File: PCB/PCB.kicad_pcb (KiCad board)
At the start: 2 copper layers, 26 x 49 mm, 8 parts, among them IC1 MSPM0G3507SPTR, J1 ICS43434 Breakout, J2 MAX98357_Breakout, J4 LED_Header, J5 MSPM0 Programming Header, J6 USBC_Power_Breakout, U2 254

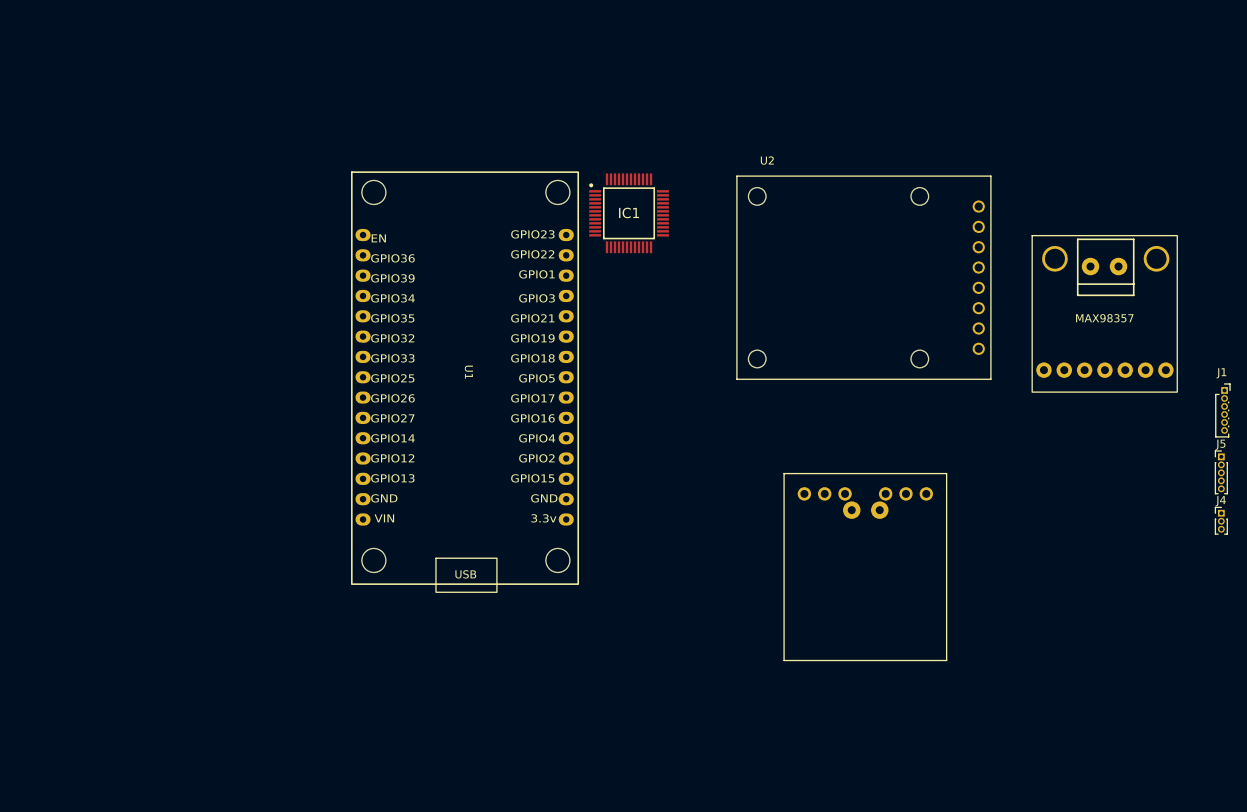
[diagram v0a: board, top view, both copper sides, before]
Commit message: all symbols and footprints
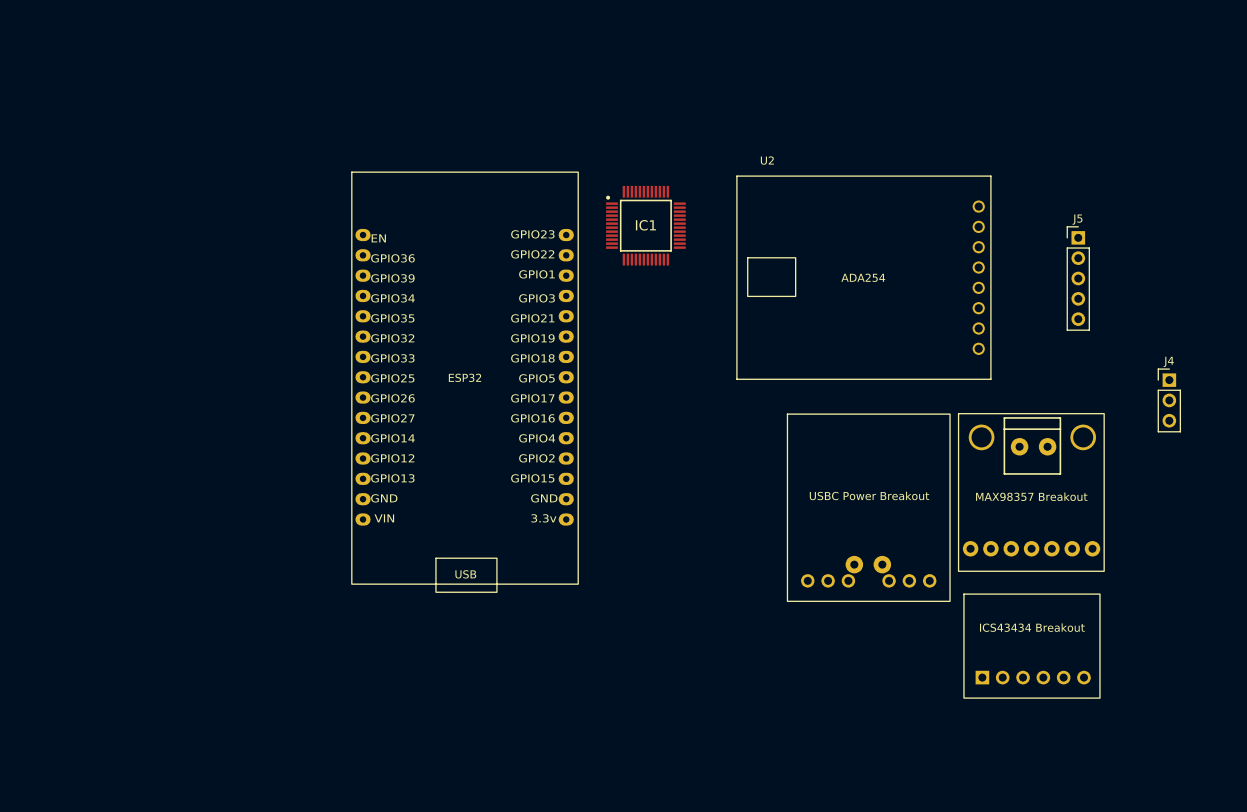
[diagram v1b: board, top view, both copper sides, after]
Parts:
- IC1: value MSPM0G3507SPTR -> QFP50P900X900X160-48N
- J1: footprint Connector_PinSocket_1.00mm:PinSocket_1x06_P1.00mm_Vertical -> SpinnyKitty:ICS43434 Breakout
- J4: footprint Connector_PinHeader_1.00mm:PinHeader_1x03_P1.00mm_Vertical -> Connector_PinHeader_2.54mm:PinHeader_1x03_P2.54mm_Vertical
- J5: footprint Connector_PinHeader_1.00mm:PinHeader_1x05_P1.00mm_Vertical -> Connector_PinHeader_2.54mm:PinHeader_1x05_P2.54mm_Vertical
- moved J1 38.2 mm to (139.5, 89.0)
- moved J5 32.7 mm to (145.3, 40.2)
- moved J2 24.1 mm to (139.4, 66.1)
- moved J4 17.9 mm to (156.7, 58.0)
- moved J6 6.82 mm to (119.1, 81.1), turned to 0 degrees
- moved IC1 2.61 mm to (91.2, 38.7)
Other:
- board outline removed

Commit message: schematic for on board power system
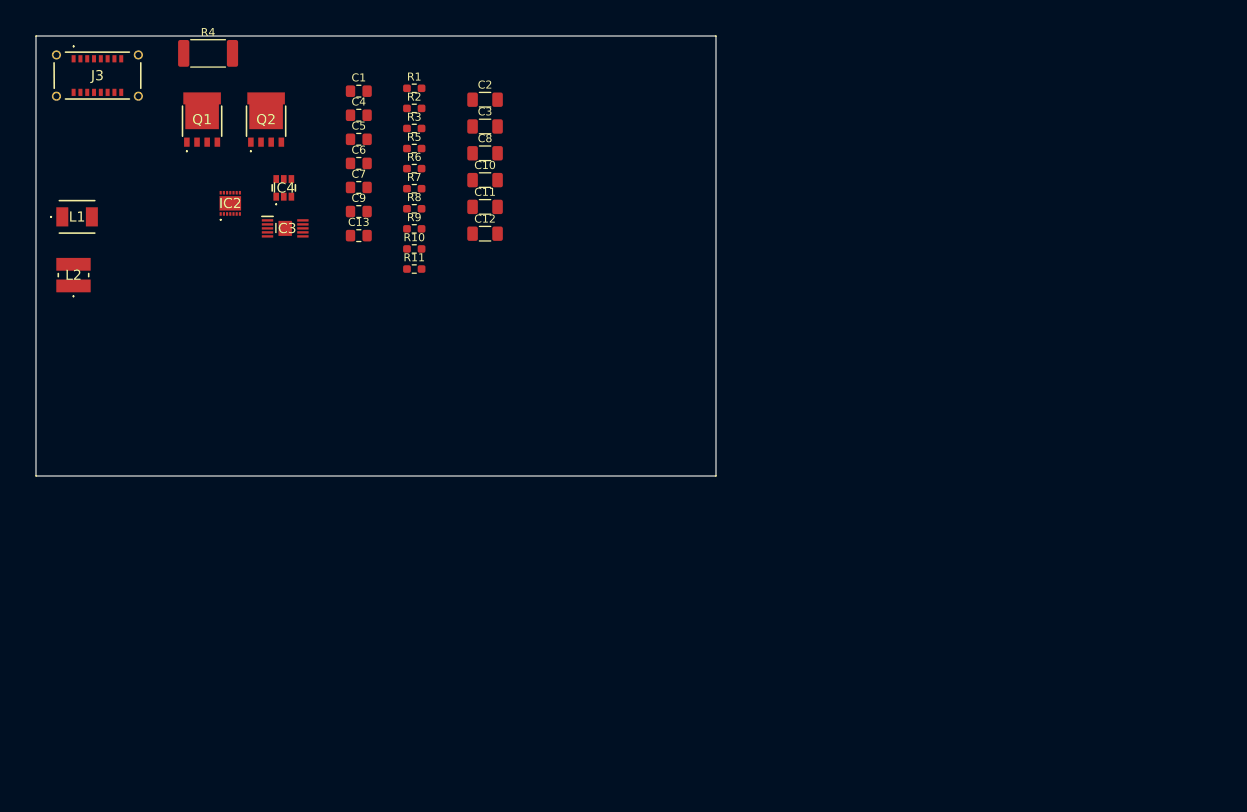
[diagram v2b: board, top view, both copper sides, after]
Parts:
- removed IC1: QFP50P900X900X160-48N, SpinnyKitty:MSPM0G3507SPTR
- removed J1: ICS43434 Breakout, SpinnyKitty:ICS43434 Breakout
- removed J2: MAX98357_Breakout, SpinnyKitty:MAX98357
- removed J4: LED_Header, Connector_PinHeader_2.54mm:PinHeader_1x03_P2.54mm_Vertical
- removed J5: MSPM0 Programming Header, Connector_PinHeader_2.54mm:PinHeader_1x05_P2.54mm_Vertical
- removed J6: USBC_Power_Breakout, SpinnyKitty:USBC_POWER_BREAKOUT
- removed U1: ~, SpinnyKitty:ESP32_30pin
- removed U2: 254, SpinnyKitty:MODULE_254
- added C1: 1uF, Capacitor_SMD:C_0805_2012Metric_Pad1.18x1.45mm_HandSolder, F.Cu at (55.4, 21.9)
- added C10: 10uF, Capacitor_SMD:C_1206_3216Metric_Pad1.33x1.80mm_HandSolder, F.Cu at (71.1, 33.0)
- added C11: 22uF, Capacitor_SMD:C_1206_3216Metric_Pad1.33x1.80mm_HandSolder, F.Cu at (71.1, 36.4)
- added C12: 22uF, Capacitor_SMD:C_1206_3216Metric_Pad1.33x1.80mm_HandSolder, F.Cu at (71.1, 39.7)
- added C13: 100nF, Capacitor_SMD:C_0805_2012Metric_Pad1.18x1.45mm_HandSolder, F.Cu at (55.4, 40.0)
- added C2: 10uF, Capacitor_SMD:C_1206_3216Metric_Pad1.33x1.80mm_HandSolder, F.Cu at (71.1, 23.0)
- added C3: 10uF, Capacitor_SMD:C_1206_3216Metric_Pad1.33x1.80mm_HandSolder, F.Cu at (71.1, 26.3)
- added C4: 4.7uF, Capacitor_SMD:C_0805_2012Metric_Pad1.18x1.45mm_HandSolder, F.Cu at (55.4, 24.9)
- added C5: 0.1uF, Capacitor_SMD:C_0805_2012Metric_Pad1.18x1.45mm_HandSolder, F.Cu at (55.4, 27.9)
- added C6: 1uF, Capacitor_SMD:C_0805_2012Metric_Pad1.18x1.45mm_HandSolder, F.Cu at (55.4, 30.9)
- added C7: 10nF, Capacitor_SMD:C_0805_2012Metric_Pad1.18x1.45mm_HandSolder, F.Cu at (55.4, 33.9)
- added C8: 22uF, Capacitor_SMD:C_1206_3216Metric_Pad1.33x1.80mm_HandSolder, F.Cu at (71.1, 29.7)
- added C9: 10pF, Capacitor_SMD:C_0805_2012Metric_Pad1.18x1.45mm_HandSolder, F.Cu at (55.4, 36.9)
- added IC2: AP33771CFBZ-13-FA01, SpinnyKitty:AP33771CFBZ13FA01, F.Cu at (39.3, 35.9)
- added IC3: LT8609EMSE#PBF, SpinnyKitty:SOP50P490X110-11N, F.Cu at (46.1, 39.0)
- added IC4: AP63203WU-7, SpinnyKitty:AP63203WU7, F.Cu at (46.0, 34.0)
- added J3: UJ20-C-V-SMT-TR-68, SpinnyKitty:UJ20CVSMTTR68, F.Cu at (22.7, 19.9)
- added L1: 2.2uH, SpinnyKitty:PM5402222NLT, F.Cu at (20.1, 37.6)
- added L2: 3.9uH, SpinnyKitty:SRR3818A3R9Y, F.Cu at (19.7, 44.9)
- added Q1: PSMN2R6-30YLC,115, SpinnyKitty:PSMN2R630YLC115, F.Cu at (35.8, 25.6)
- added Q2: PSMN2R6-30YLC,115, SpinnyKitty:PSMN2R630YLC115, F.Cu at (43.8, 25.6)
- added R1: 5.1k, Resistor_SMD:R_0603_1608Metric_Pad0.98x0.95mm_HandSolder, F.Cu at (62.3, 21.5)
- added R10: 187k, Resistor_SMD:R_0603_1608Metric_Pad0.98x0.95mm_HandSolder, F.Cu at (62.3, 41.6)
- added R11: 1M, Resistor_SMD:R_0603_1608Metric_Pad0.98x0.95mm_HandSolder, F.Cu at (62.3, 44.1)
- added R2: 5.1k, Resistor_SMD:R_0603_1608Metric_Pad0.98x0.95mm_HandSolder, F.Cu at (62.3, 24.0)
- added R3: 6.2k, Resistor_SMD:R_0603_1608Metric_Pad0.98x0.95mm_HandSolder, F.Cu at (62.3, 26.6)
- added R4: 5m, Resistor_SMD:R_2512_6332Metric_Pad1.40x3.35mm_HandSolder, F.Cu at (36.5, 17.2)
- added R5: 200, Resistor_SMD:R_0603_1608Metric_Pad0.98x0.95mm_HandSolder, F.Cu at (62.3, 29.1)
- added R6: 66k, Resistor_SMD:R_0603_1608Metric_Pad0.98x0.95mm_HandSolder, F.Cu at (62.3, 31.6)
- added R7: 5.1k, Resistor_SMD:R_0603_1608Metric_Pad0.98x0.95mm_HandSolder, F.Cu at (62.3, 34.1)
- added R8: 100k, Resistor_SMD:R_0603_1608Metric_Pad0.98x0.95mm_HandSolder, F.Cu at (62.3, 36.6)
- added R9: 18.2k, Resistor_SMD:R_0603_1608Metric_Pad0.98x0.95mm_HandSolder, F.Cu at (62.3, 39.1)
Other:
- board outline added: 85 x 55 mm

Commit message: backup power rail pcb
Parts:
- added C14: 0.1uF, Capacitor_SMD:C_0805_2012Metric_Pad1.18x1.45mm_HandSolder, F.Cu at (100.8, 39.0)
- added C15: 47uF, Capacitor_SMD:C_0805_2012Metric_Pad1.18x1.45mm_HandSolder, F.Cu at (96.8, 38.9)
- added C16: 0.1uF, Capacitor_SMD:C_0805_2012Metric_Pad1.18x1.45mm_HandSolder, F.Cu at (83.7, 50.4)
- added C17: 47uF, Capacitor_SMD:C_0805_2012Metric_Pad1.18x1.45mm_HandSolder, F.Cu at (83.7, 46.4)
- added C18: 0.1uF, Capacitor_SMD:C_0805_2012Metric_Pad1.18x1.45mm_HandSolder, F.Cu at (88.4, 68.7)
- added C19: 22uF, Capacitor_SMD:C_1206_3216Metric_Pad1.33x1.80mm_HandSolder, F.Cu at (88.3, 63.7)
- added J6: USBC_Power_Breakout, SpinnyKitty:USBC_POWER_BREAKOUT, F.Cu at (97.6, 33.2)
- added J7: ~, Connector_PinHeader_2.54mm:PinHeader_1x04_P2.54mm_Vertical, F.Cu at (109.7, 56.4)
- added U3: ~, SpinnyKitty:5V 3A Buck, F.Cu at (96.0, 48.8)
- added U4: ~, SpinnyKitty:3V3 1.8A Buck, F.Cu at (98.6, 66.2)
- C13: value 100nF -> 0.1uF
- moved L1 97.6 mm to (115.7, 57.1)
- moved L2 95.2 mm to (109.0, 77.9)
- moved J3 94.9 mm to (117.6, 21.7), turned to 90 degrees
- moved R4 89.9 mm to (124.3, 36.6), turned to 180 degrees
- moved Q1 89.3 mm to (123.1, 44.3)
- moved IC3 81.4 mm to (124.7, 60.3)
- moved IC2 80.8 mm to (119.9, 31.3), turned to 90 degrees
- moved C7 77.5 mm to (126.3, 65.1)
- moved C4 76.5 mm to (124.7, 57.1), turned to 180 degrees
- moved Q2 74.8 mm to (115.6, 46.6)
- moved C9 74.1 mm to (122.1, 69.1)
- moved C5 71.7 mm to (120.3, 58.3), turned to -90 degrees
- moved C6 71.3 mm to (119.3, 62.3), turned to 90 degrees
- moved R8 71.0 mm to (126.3, 67.4)
- moved IC4 70.7 mm to (100.8, 78.6), turned to -90 degrees
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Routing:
- net GND: track 0.00 -> 217.6 mm, vias 0 -> 11
- net +5V: track 0.00 -> 112.1 mm
- net +12V: track 0.00 -> 84.3 mm
- net +3V3: track 0.00 -> 64.1 mm
- net /VBUS: track 0.00 -> 48.8 mm, vias 0 -> 4
- net /DP: track 0.00 -> 25.0 mm, vias 0 -> 3
- net /DN: track 0.00 -> 21.6 mm, vias 0 -> 3
- net /GATE_DRV: track 0.00 -> 20.6 mm
- net Net-(IC3-FB): track 0.00 -> 16.8 mm
- net /IC_CC2: track 0.00 -> 15.0 mm
- net /IC_CC1: track 0.00 -> 13.9 mm
- net /VBUS_SW_IN: track 0.00 -> 13.6 mm
- net /FET_MID: track 0.00 -> 13.5 mm, vias 0 -> 2
- net /POWER GOOD: track 0.00 -> 9.95 mm
- net Net-(IC2-VOUT): track 0.00 -> 9.28 mm
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- added copper zone on B.Cu, net GND
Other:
- board size 85 x 55 mm -> 119.9 x 90.3 mm
- board text added: "12V"
- board text added: "12V USBC Input"
- board text added: "12V->5V Buck (3A)"
- board text added: "3V3"
- board text added: "5V"
- board text added: "5V->3V Buck (2A)"
- board text added: "GND"
- board text added: "^^^"
